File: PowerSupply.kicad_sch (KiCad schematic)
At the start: 8 parts, among them U501 TPSM33625

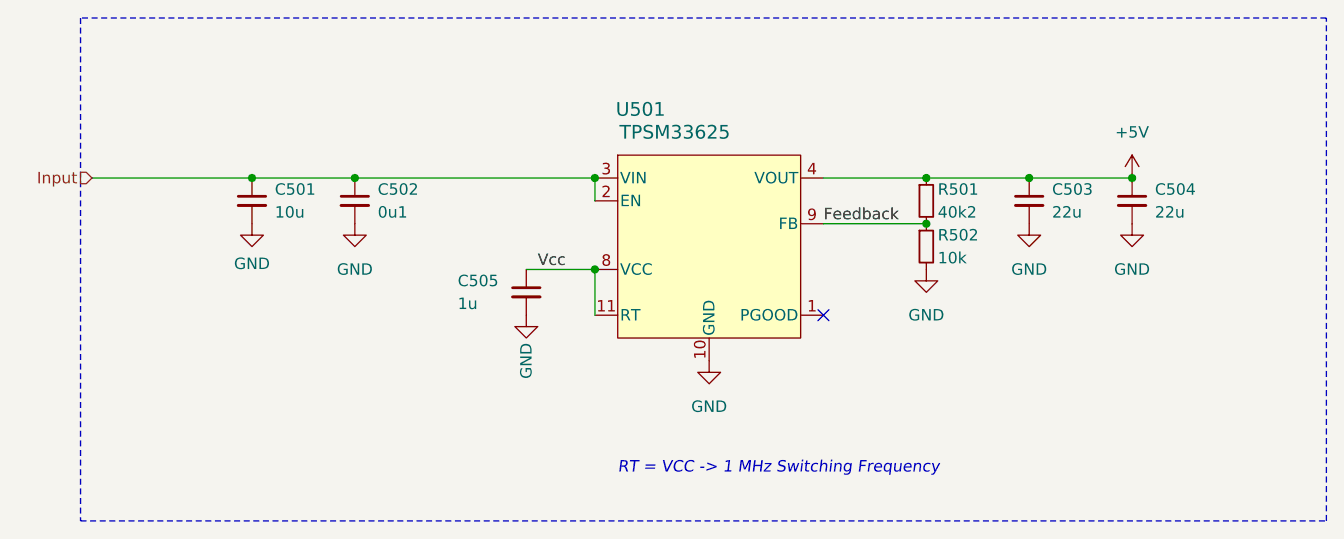
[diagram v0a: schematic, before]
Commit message: Replace Order_Number
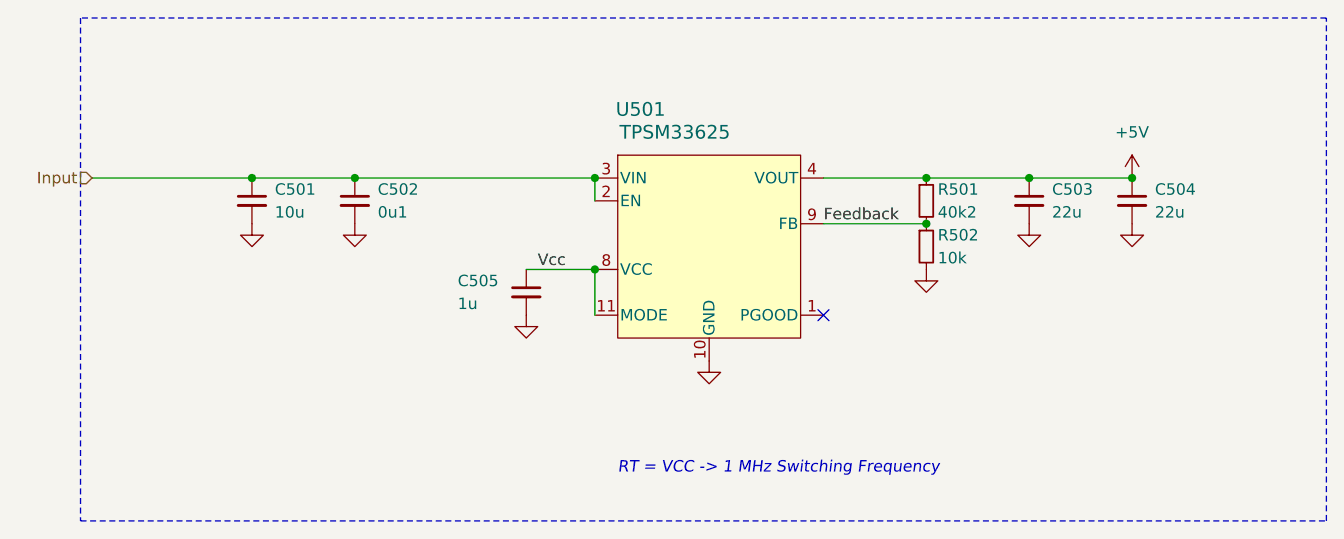
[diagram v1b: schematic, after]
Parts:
- C501: footprint Capacitor_SMD:C_1210_3225Metric -> V2_Capacitor_SMD:C_1210; symbol Device:C_Small -> V2_Device:C_1210_10u; Manufacturer (none) -> TDK; Mouser (none) -> 810-CNA6P1X7R1H106K2; Product (none) -> CNA6P1X7R1H106K250AE; Rating (none) -> 50V
- C502: footprint Capacitor_SMD:C_0603_1608Metric -> V2_Capacitor_SMD:C_0603; symbol Device:C_Small -> V2_Device:C_0603_0u1; Manufacturer (none) -> TDK; Mouser (none) -> 810-CGA3E2X7R1H104MA; Product (none) -> CGA3E2X7R1H104M080AA; Rating (none) -> 50V
- C503, C504: footprint Capacitor_SMD:C_1210_3225Metric -> V2_Capacitor_SMD:C_1210; symbol Device:C_Small -> V2_Device:C_1210_22u; Manufacturer (none) -> TDK; Mouser (none) -> 810-CGA6P3X7R1E226M5; Product (none) -> CGA6P3X7R1E226M250AE; Rating (none) -> 25V
- C505: footprint Capacitor_SMD:C_0603_1608Metric -> V2_Capacitor_SMD:C_0603; symbol Device:C_Small -> V2_Device:C_0603_1u; Manufacturer (none) -> TDK; Mouser (none) -> 810-CGA3E3X7R1H105K0; Product (none) -> CGA3E3X7R1H105K080AB; Rating (none) -> 50V
- R501: footprint Resistor_SMD:R_0603_1608Metric -> V2_Resistor_SMD:R_0603; symbol Device:R_Small -> V2_Device:R_0603_40k2; Manufacturer (none) -> Vishay; Mouser (none) -> 71-RCS060340K2FKEA; Product (none) -> RCS060340K2FKEA; Rating (none) -> 500mW
- R502: footprint Resistor_SMD:R_0603_1608Metric -> V2_Resistor_SMD:R_0603; symbol Device:R_Small -> V2_Device:R_0603_10k; Manufacturer (none) -> Vishay; Mouser (none) -> 71-CRCW060310K0FKEAC; Product (none) -> CRCW060310K0FKEAC; Rating (none) -> 100mW
- U501: footprint V2_Converter_DCDC:TPSM33625 -> V2_Converter_DCDC:QFN-11; symbol V2_Converter_DCDC:TPSM33625 -> V2_Converter_DCDC:TPSM33625RDNR; Manufacturer (none) -> Texas Instruments; Mouser (none) -> 595-TPSM33625RDNR; Product (none) -> TPSM33625RDNR; Rating (none) -> 2.5A

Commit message: Update Library
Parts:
- C501: symbol V2_Device:C_1210_10u -> V2_Capacitor:1210_10u
- C502: symbol V2_Device:C_0603_0u1 -> V2_Capacitor:0603_0u1
- C503, C504: value 22u -> 10u; symbol V2_Device:C_1210_22u -> V2_Capacitor:1210_22u
- C505: symbol V2_Device:C_0603_1u -> V2_Capacitor:0603_1u
- R501: symbol V2_Device:R_0603_40k2 -> V2_Resistor:0603_40k2
- R502: symbol V2_Device:R_0603_10k -> V2_Resistor:0603_10k
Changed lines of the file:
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@@
 		(on_board yes)
 		(dnp no)
-		(property "Reference" "#PWR0504"
+		(property "Reference" "#PWR504"
 			(at 194.31 107.95 0)
 			(effects
@@
 			(project "control"
 				(path "/6c8448b4-b04d-47e1-934e-e40cbe27a7be/24a9dc0c-cb3c-464a-a734-f09bf949d71a"
-					(reference "#PWR0504")
+					(reference "#PWR504")
 					(unit 1)
 				)
@@
 		(on_board yes)
 		(dnp no)
-		(property "Reference" "#PWR0507"
+		(property "Reference" "#PWR507"
 			(at 138.43 118.11 0)
 			(effects
@@
 			(project "control"
 				(path "/6c8448b4-b04d-47e1-934e-e40cbe27a7be/24a9dc0c-cb3c-464a-a734-f09bf949d71a"
-					(reference "#PWR0507")
-					(unit 1)
-				)
-			)
-		)
-	)
-	(symbol
-		(lib_id "V2_Device:R_0603_10k")
+					(reference "#PWR507")
+					(unit 1)
+				)
+			)
+		)
+	)
+	(symbol
+		(lib_id "V2_Resistor:0603_10k")
 		(at 182.88 104.14 0)
 		(unit 1)
@@
 	)
 	(symbol
-		(lib_id "V2_Device:R_0603_40k2")
+		(lib_id "V2_Resistor:0603_40k2")
 		(at 182.88 99.06 0)
 		(unit 1)
@@
 		(on_board yes)
 		(dnp no)
-		(property "Reference" "#PWR0506"
+		(property "Reference" "#PWR506"
 			(at 182.88 113.03 0)
 			(effects
@@
 			(project "control"
 				(path "/6c8448b4-b04d-47e1-934e-e40cbe27a7be/24a9dc0c-cb3c-464a-a734-f09bf949d71a"
-					(reference "#PWR0506")
+					(reference "#PWR506")
 					(unit 1)
 				)
@@
 		(on_board yes)
 		(dnp no)
-		(property "Reference" "#PWR0503"
+		(property "Reference" "#PWR503"
 			(at 119.38 107.95 0)
 			(effects
@@
 			(project "control"
 				(path "/6c8448b4-b04d-47e1-934e-e40cbe27a7be/24a9dc0c-cb3c-464a-a734-f09bf949d71a"
-					(reference "#PWR0503")
-					(unit 1)
-				)
-			)
-		)
-	)
-	(symbol
-		(lib_id "V2_Device:C_1210_10u")
+					(reference "#PWR503")
+					(unit 1)
+				)
+			)
+		)
+	)
+	(symbol
+		(lib_id "V2_Capacitor:1210_10u")
 		(at 107.95 99.06 0)
 		(unit 1)
@@
 	)
 	(symbol
-		(lib_id "V2_Device:C_0603_1u")
+		(lib_id "V2_Capacitor:0603_1u")
 		(at 138.43 109.22 0)
 		(unit 1)
@@
 	)
 	(symbol
-		(lib_id "V2_Device:C_1210_22u")
+		(lib_id "V2_Capacitor:1210_22u")
 		(at 194.31 99.06 0)
 		(unit 1)
@@
 			)
 		)
-		(property "Value" "22u"
+		(property "Value" "10u"
 			(at 196.85 100.33 0)
 			(effects
@@
 	)
 	(symbol
-		(lib_id "V2_Device:C_0603_0u1")
+		(lib_id "V2_Capacitor:0603_0u1")
 		(at 119.38 99.06 0)
 		(unit 1)
@@
 		(on_board yes)
 		(dnp no)
-		(property "Reference" "#PWR0502"
+		(property "Reference" "#PWR502"
 			(at 107.95 107.95 0)
 			(effects
@@
 			(project "control"
 				(path "/6c8448b4-b04d-47e1-934e-e40cbe27a7be/24a9dc0c-cb3c-464a-a734-f09bf949d71a"
-					(reference "#PWR0502")
+					(reference "#PWR502")
 					(unit 1)
 				)
@@
 		(on_board yes)
 		(dnp no)
-		(property "Reference" "#PWR0505"
+		(property "Reference" "#PWR505"
 			(at 205.74 107.95 0)
 			(effects
@@
 			(project "control"
 				(path "/6c8448b4-b04d-47e1-934e-e40cbe27a7be/24a9dc0c-cb3c-464a-a734-f09bf949d71a"
-					(reference "#PWR0505")
+					(reference "#PWR505")
 					(unit 1)
 				)
@@
 		(on_board yes)
 		(dnp no)
-		(property "Reference" "#PWR0501"
+		(property "Reference" "#PWR501"
 			(at 205.74 100.33 0)
 			(effects
@@
 			(project "control"
 				(path "/6c8448b4-b04d-47e1-934e-e40cbe27a7be/24a9dc0c-cb3c-464a-a734-f09bf949d71a"
-					(reference "#PWR0501")
+					(reference "#PWR501")
 					(unit 1)
 				)
@@
 		(on_board yes)
 		(dnp no)
-		(property "Reference" "#PWR0508"
+		(property "Reference" "#PWR508"
 			(at 158.75 123.19 0)
 			(effects
@@
 			(project "control"
 				(path "/6c8448b4-b04d-47e1-934e-e40cbe27a7be/24a9dc0c-cb3c-464a-a734-f09bf949d71a"
-					(reference "#PWR0508")
-					(unit 1)
-				)
-			)
-		)
-	)
-	(symbol
-		(lib_id "V2_Device:C_1210_22u")
+					(reference "#PWR508")
+					(unit 1)
+				)
+			)
+		)
+	)
+	(symbol
+		(lib_id "V2_Capacitor:1210_22u")
 		(at 205.74 99.06 0)
 		(unit 1)
@@
 			)
 		)
-		(property "Value" "22u"
+		(property "Value" "10u"
 			(at 208.28 100.33 0)
 			(effects

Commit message: Refresh
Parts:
- C503, C504: value 10u -> 22u
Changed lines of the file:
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@@
 			)
 		)
-		(property "Value" "10u"
+		(property "Value" "22u"
 			(at 196.85 100.33 0)
 			(effects
@@
 			)
 		)
-		(property "Value" "10u"
+		(property "Value" "22u"
 			(at 208.28 100.33 0)
 			(effects

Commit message: Update ESD suppressor
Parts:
- C501: Mouser 810-CNA6P1X7R1H106K2 -> 810-CNC6P1X7R1H106K2; Product CNA6P1X7R1H106K250AE -> CNC6P1X7R1H106K250AE
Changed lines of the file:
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@@
 			)
 		)
-		(property "Description" "Resistor, small symbol"
+		(property "Description" ""
 			(at 182.88 116.84 0)
 			(effects
@@
 			)
 		)
-		(property "Description" "Resistor, small symbol"
+		(property "Description" ""
 			(at 182.88 111.76 0)
 			(effects
@@
 			)
 		)
-		(property "Description" "Unpolarized capacitor, small symbol"
+		(property "Description" ""
 			(at 107.95 111.76 0)
 			(effects
@@
 			)
 		)
-		(property "Mouser" "810-CNA6P1X7R1H106K2"
+		(property "Mouser" "810-CNC6P1X7R1H106K2"
 			(at 107.95 121.92 0)
 			(effects
@@
 			)
 		)
-		(property "Product" "CNA6P1X7R1H106K250AE"
+		(property "Product" "CNC6P1X7R1H106K250AE"
 			(at 107.95 116.84 0)
 			(effects
@@
 			)
 		)
-		(property "Description" "Unpolarized capacitor, small symbol"
+		(property "Description" ""
 			(at 138.43 121.92 0)
 			(effects
@@
 			)
 		)
-		(property "Description" "Unpolarized capacitor, small symbol"
+		(property "Description" ""
 			(at 194.31 111.76 0)
 			(effects
@@
 			)
 		)
-		(property "Description" "Unpolarized capacitor, small symbol"
+		(property "Description" ""
 			(at 119.38 111.76 0)
 			(effects
@@
 			)
 		)
-		(property "Description" "Unpolarized capacitor, small symbol"
+		(property "Description" ""
 			(at 205.74 111.76 0)
 			(effects

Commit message: Replace diode
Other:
- title: Power Supply -> V2 control

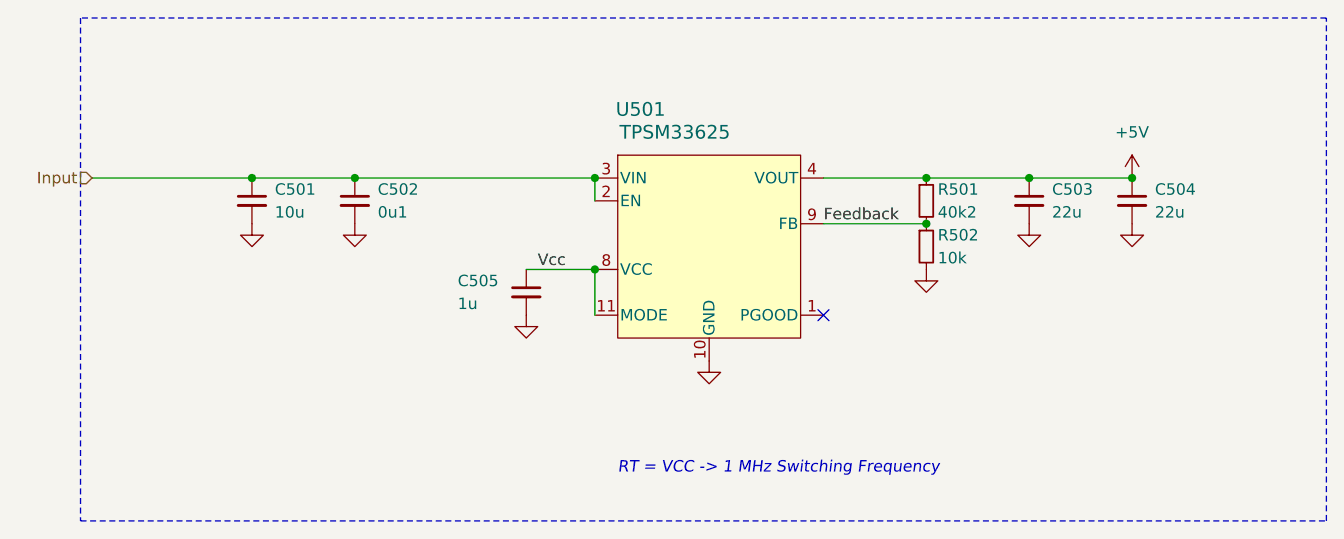
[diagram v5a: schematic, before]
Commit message: Replace step-down
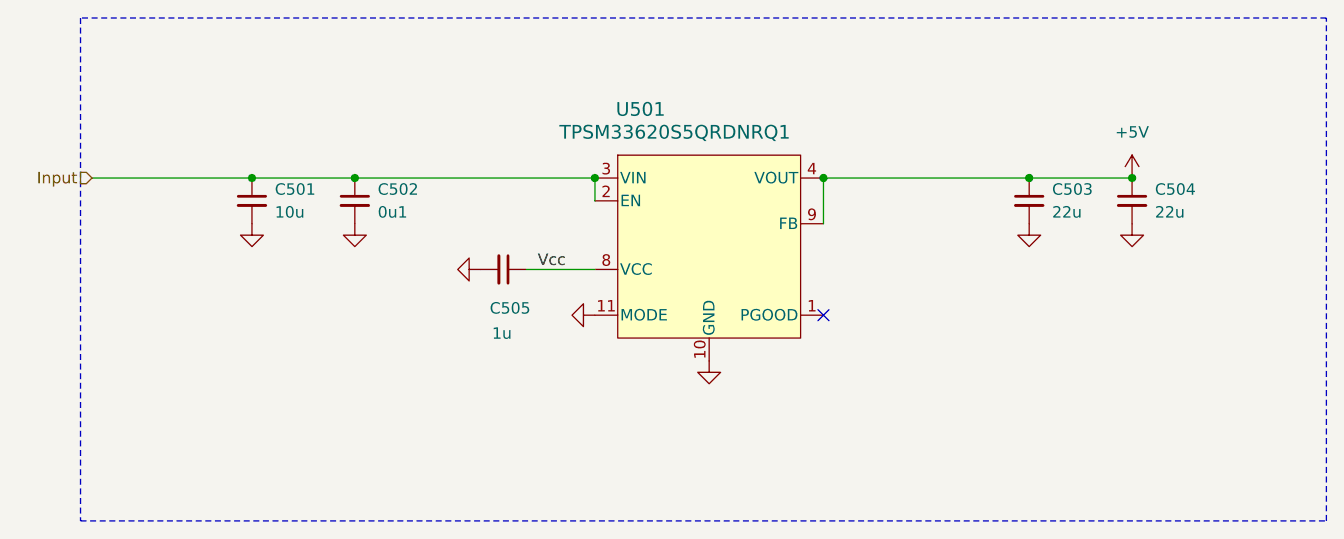
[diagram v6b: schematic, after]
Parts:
- removed R501: 40k2, V2_Resistor_SMD:R_0603, symbol V2_Resistor:0603_40k2
- removed R502: 10k, V2_Resistor_SMD:R_0603, symbol V2_Resistor:0603_10k
- U501: value TPSM33625 -> TPSM33620S5QRDNRQ1; symbol V2_Converter_DCDC:TPSM33625RDNR -> V2_Converter_DCDC:TPSM33620S5QRDNRQ1; Mouser 595-TPSM33625RDNR -> 595-SM33620S5QRDNRQ1; Product TPSM33625RDNR -> TPSM33620S5QRDNRQ1; Rating 2.5A -> 2A
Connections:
- net Feedback is gone; now on net +5V: U501.9 (FB)
- net GND: now also U501.11 (MODE)
- net Vcc: no longer U501.11 (MODE)
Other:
- note removed: "RT = VCC -> 1 MHz Switching Frequency"
- moved on the sheet: C505

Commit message: Good Bye Imperial
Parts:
- C501: footprint V2_Capacitor_SMD:C_1210 -> V2_Capacitor_SMD:C_3225; symbol V2_Capacitor:1210_10u -> V2_Capacitor:3225_10u
- C502: footprint V2_Capacitor_SMD:C_0603 -> V2_Capacitor_SMD:C_1608; symbol V2_Capacitor:0603_0u1 -> V2_Capacitor:1608_0u1
- C503, C504: footprint V2_Capacitor_SMD:C_1210 -> V2_Capacitor_SMD:C_3225; symbol V2_Capacitor:1210_22u -> V2_Capacitor:3225_22u
- C505: footprint V2_Capacitor_SMD:C_0603 -> V2_Capacitor_SMD:C_1608; symbol V2_Capacitor:0603_1u -> V2_Capacitor:1608_1u
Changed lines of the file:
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@@
 	)
 	(symbol
-		(lib_id "V2_Capacitor:1210_10u")
+		(lib_id "V2_Capacitor:3225_10u")
 		(at 107.95 99.06 0)
 		(unit 1)
@@
 			)
 		)
-		(property "Footprint" "V2_Capacitor_SMD:C_1210"
+		(property "Footprint" "V2_Capacitor_SMD:C_3225"
 			(at 107.95 116.078 0)
 			(hide yes)
@@
 	)
 	(symbol
-		(lib_id "V2_Capacitor:0603_1u")
+		(lib_id "V2_Capacitor:1608_1u")
 		(at 135.89 106.68 270)
 		(unit 1)
@@
 			)
 		)
-		(property "Footprint" "V2_Capacitor_SMD:C_0603"
+		(property "Footprint" "V2_Capacitor_SMD:C_1608"
 			(at 118.872 106.68 0)
 			(hide yes)
@@
 	)
 	(symbol
-		(lib_id "V2_Capacitor:1210_22u")
+		(lib_id "V2_Capacitor:3225_22u")
 		(at 194.31 99.06 0)
 		(unit 1)
@@
 			)
 		)
-		(property "Footprint" "V2_Capacitor_SMD:C_1210"
+		(property "Footprint" "V2_Capacitor_SMD:C_3225"
 			(at 194.31 116.078 0)
 			(hide yes)
@@
 	)
 	(symbol
-		(lib_id "V2_Capacitor:0603_0u1")
+		(lib_id "V2_Capacitor:1608_0u1")
 		(at 119.38 99.06 0)
 		(unit 1)
@@
 			)
 		)
-		(property "Footprint" "V2_Capacitor_SMD:C_0603"
+		(property "Footprint" "V2_Capacitor_SMD:C_1608"
 			(at 119.38 116.078 0)
 			(hide yes)
@@
 	)
 	(symbol
-		(lib_id "V2_Capacitor:1210_22u")
+		(lib_id "V2_Capacitor:3225_22u")
 		(at 205.74 99.06 0)
 		(unit 1)
@@
 			)
 		)
-		(property "Footprint" "V2_Capacitor_SMD:C_1210"
+		(property "Footprint" "V2_Capacitor_SMD:C_3225"
 			(at 205.74 116.078 0)
 			(hide yes)
